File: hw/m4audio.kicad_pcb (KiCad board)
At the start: 2 copper layers, 49.7 x 49.7 mm, 95 parts, among them J1 JACK_TRS, J11 CONN_01X03, J2 JACK_TRS, J21 CONN_01X03, P1 CONN_01X02, P2 USB_OTG, P3 CONN_02X05, P4 CONN_01X08, P5 CONN_01X03, P6 CONN_01X04, U1 LD1117S33TR, U2 STM32F405RG, U3 AD8542, U4 WM8731, Y1 Crystal

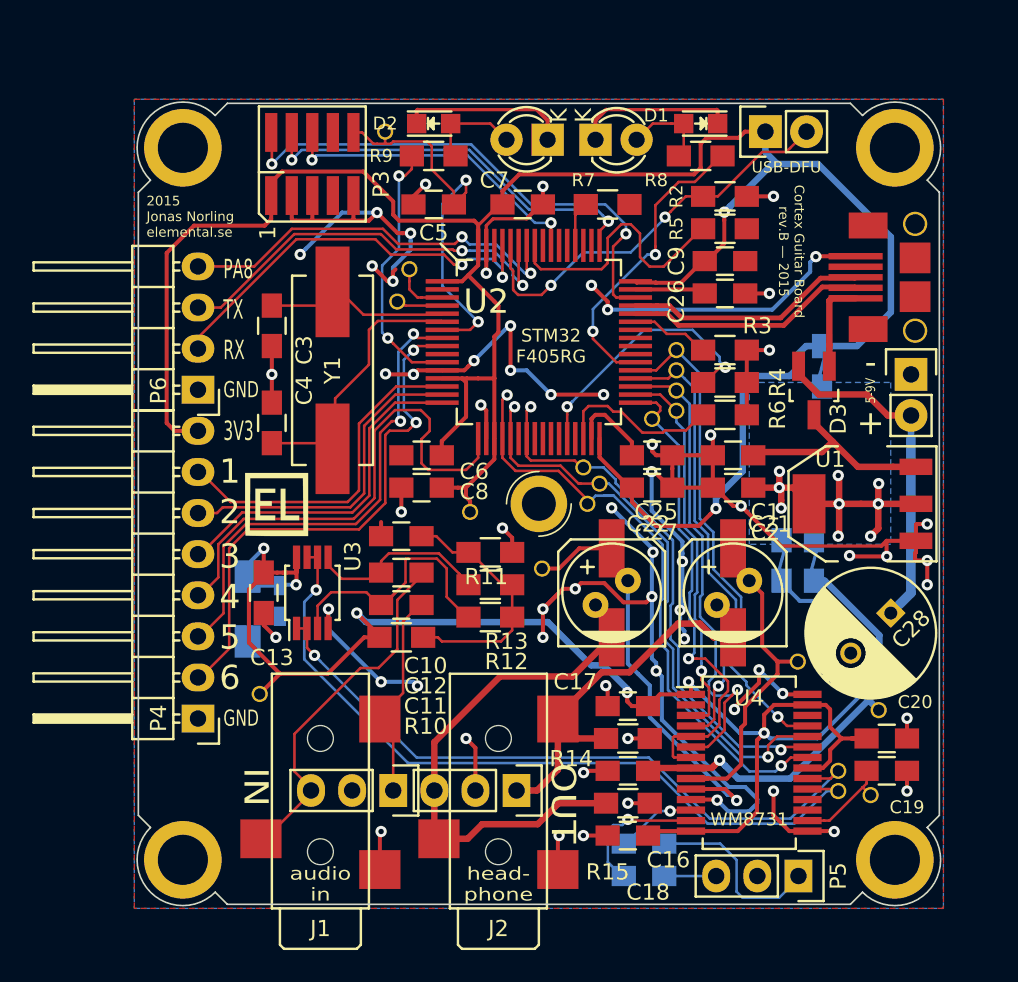
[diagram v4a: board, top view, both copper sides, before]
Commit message: Change LED footprints and resistors, RST header, hole in GND pad
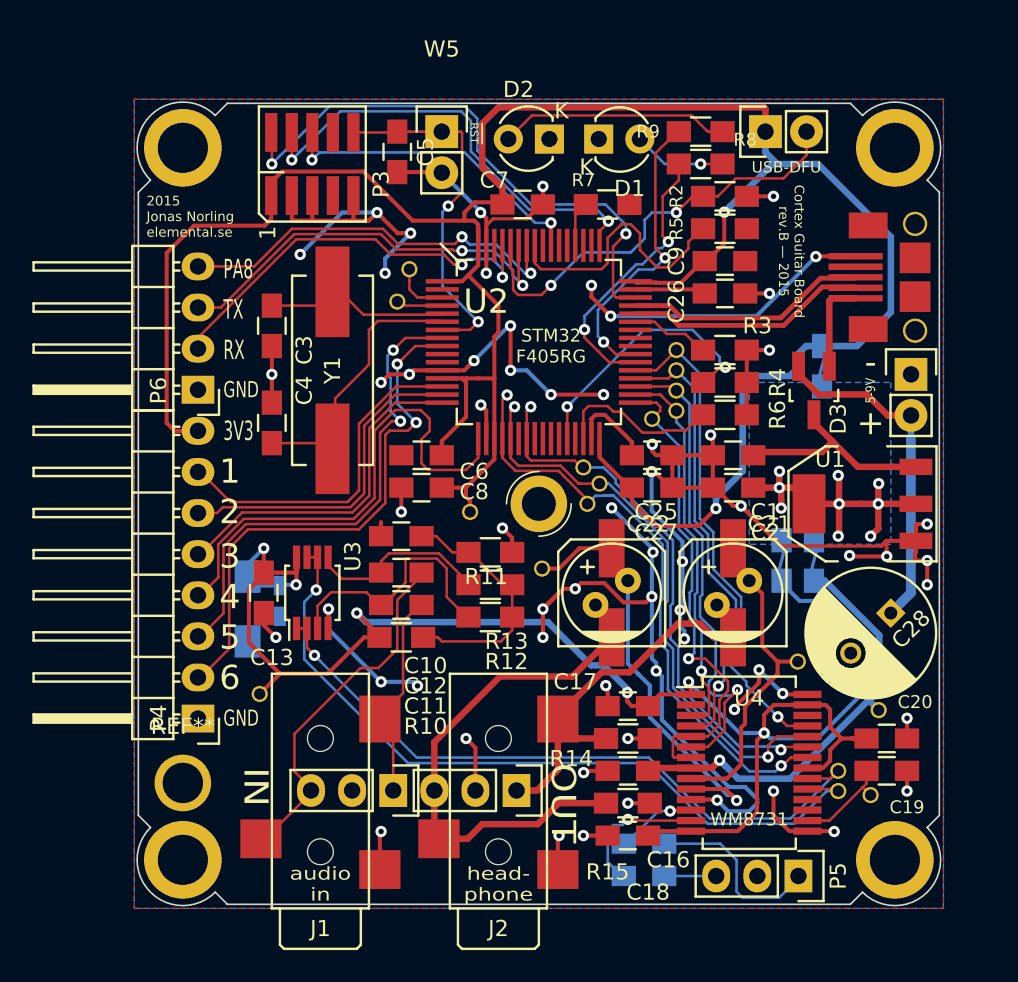
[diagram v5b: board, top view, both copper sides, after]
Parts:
- removed D11: green, LEDs:LED-3MM
- removed D21: orange, LEDs:LED-3MM
- removed G***: LOGO, elemental:elemental-25.4mm
- removed G***: LOGO, elemental:elemental-4mm
- removed G***: LOGO, Jonas_Gnomes:OSHW_4mm_mask
- removed G***: LOGO, elemental:elemental-4mm-mask
- removed the REF** at (130.0, 126.0)
- removed TP19: TST, Jonas_Connectors:TP_0.7mm
- added REF**: MountingHole_2-5mm, Mounting_Holes:MountingHole_2-5mm, F.Cu at (114.0, 132.2)
- added W5: TEST, Pin_Headers:Pin_Header_Straight_1x02, F.Cu at (130.0, 92.0)
- D1, D2: footprint LEDs:LED-0805 -> Footprints:LED-3MM
- moved R9 16.6 mm to (146.0, 92.0)
- moved D2 7.22 mm to (136.7, 92.5), turned to 180 degrees
- moved D1 6.37 mm to (139.7, 92.5), turned to 0 degrees
- moved C5 3.95 mm to (127.2, 93.2), turned to 270 degrees
- moved R8 0.50 mm to (146.0, 94.0), turned to 180 degrees
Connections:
- U2 pad 11: /LED2 -> Net-(U2-Pad11)
- U2 pad 39: Net-(U2-Pad39) -> /LED2
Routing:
- net GND: track 237.5 -> 221.9 mm, vias 64 -> 63
- net Net-(D2-Pad2): track 5.99 -> 14.3 mm
- net VDD: track 149.9 -> 157.6 mm
- net /SWCLK: track 25.1 -> 29.0 mm
- net /SWDIO: track 32.5 -> 35.6 mm
- net /NRST: track 24.7 -> 22.3 mm
- net /LED2: track 16.4 -> 18.6 mm
- net /BOOT0: track 25.3 -> 26.8 mm
- net /LED1: track 18.8 -> 17.6 mm
- net Net-(D1-Pad2): track 5.45 -> 6.20 mm, vias 0 -> 1
- net /SWO: track 19.7 -> 20.3 mm

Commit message: Redo power supply, split ground plane
Change to using two SOT-23-5 voltage regulators, one for analog and
one for digital. Split the ground plane so that digital and analog
meat at only one point, hoping to improve ground coupled noise
performance.

Update silkscreen texts to "rev.C".

Move silkscreen texts.
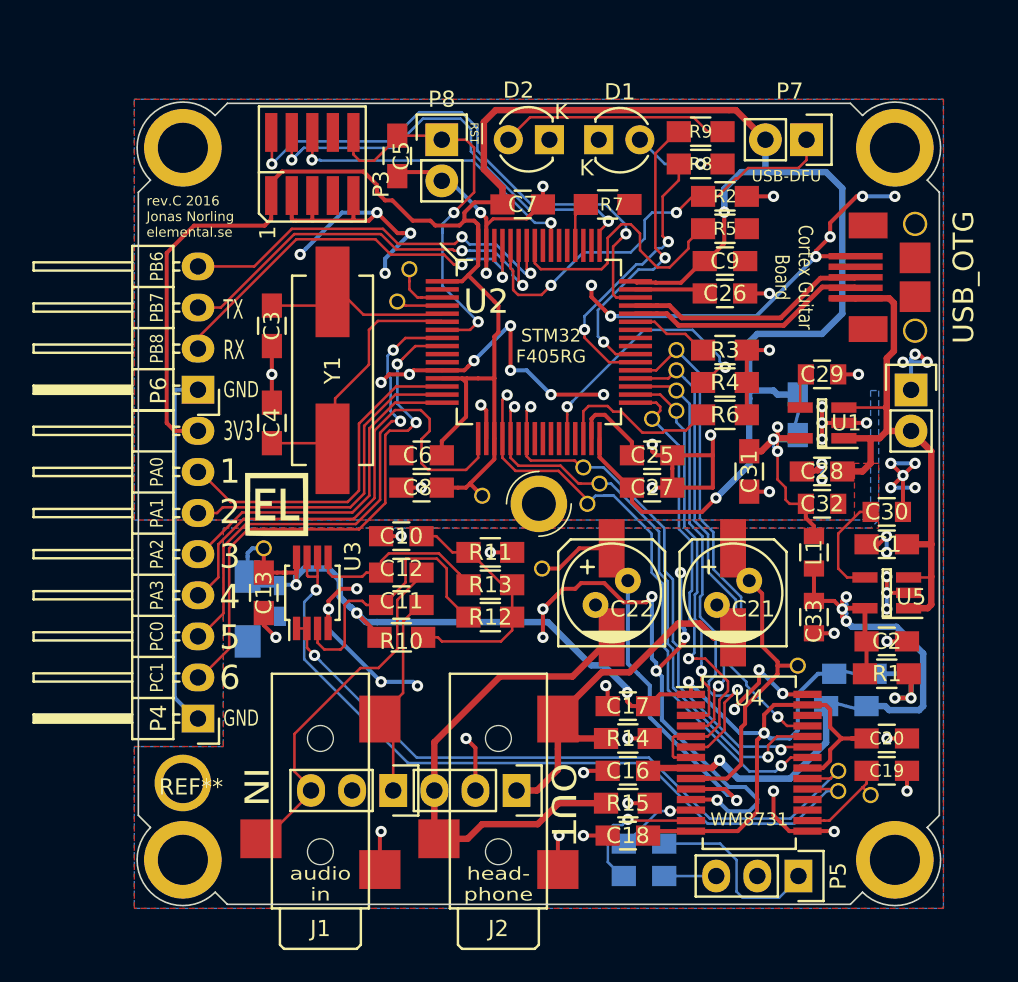
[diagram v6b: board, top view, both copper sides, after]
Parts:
- removed D3: SBAT54CLT1G, Housings_SOT-23_SOT-143_TSOT-6:SOT-23_Handsoldering
- removed TP9: TST, Jonas_Connectors:TP_0.7mm
- removed W1, W5: TEST, Pin_Headers:Pin_Header_Straight_1x02
- removed W2: V_A, Jonas_Connectors:net_tie_0805
- removed W3: V_D, Jonas_Connectors:net_tie_0805
- removed W4: V_HP, Jonas_Connectors:net_tie_0805
- added C29: 100p, Capacitors_SMD:C_0805, F.Cu at (153.5, 107.0)
- added C30: 100p, Capacitors_SMD:C_0805, F.Cu at (157.5, 115.5)
- added C31: 10u, Capacitors_SMD:C_0805_HandSoldering, F.Cu at (149.0, 113.0)
- added C32: DNP, Capacitors_SMD:C_0805, F.Cu at (153.5, 115.0)
- added C33: DNP, Capacitors_SMD:C_0805, F.Cu at (153.0, 122.0)
- added G***: LOGO, elemental:elemental-4mm, F.Cu at (119.8, 115.0)
- added G***: LOGO, elemental:elemental-25.4mm, B.Cu at (122.5, 107.2)
- added G***: LOGO, elemental:elemental-4mm-mask, B.Cu at (150.5, 99.8)
- added L1: DNP, Capacitors_SMD:C_0805, F.Cu at (153.0, 118.0)
- added P7: CONN_01X02, Pin_Headers:Pin_Header_Straight_1x02, F.Cu at (152.5, 92.5)
- added P8: CONN_01X02, Pin_Headers:Pin_Header_Straight_1x02, F.Cu at (130.0, 92.5)
- added R1: R, Resistors_SMD:R_0805_HandSoldering, F.Cu at (157.5, 125.5)
- added REF**: OSHW, Footprints:OSHW_4mm_mask, B.Cu at (146.5, 99.8)
- added REF**: gnome1, Jonas_Gnomes:gnome1, B.Cu at (136.0, 125.5)
- added TIE1: V_D, Jonas_Connectors:net_tie_0805, B.Cu at (152.0, 109.5)
- added TIE2: V_A, Jonas_Connectors:net_tie_0805, B.Cu at (155.5, 125.5)
- added TIE3: V_HP, Jonas_Connectors:net_tie_0805, B.Cu at (155.0, 127.5)
- added U5: AP2210K-3.3, Footprints:SOT-23-5_Handsoldering, F.Cu at (157.5, 120.5)
- C1: value 10u -> 10u16V
- C28: value DNP -> 10u16V; footprint Capacitors_ThroughHole:C_Radial_D8_L11.5_P3.5 -> Capacitors_SMD:C_0805_HandSoldering
- U1: value LD1117S33TR -> AP2210K-3.3; footprint SMD_Packages:SOT-223 -> Footprints:SOT-23-5_Handsoldering
- moved C2 13.4 mm to (157.5, 123.5), turned to 0 degrees
- moved C1 11.0 mm to (157.5, 117.5)
- moved C28 9.73 mm to (153.5, 113.0), turned to 180 degrees
- moved TP1 9.00 mm to (119.0, 117.8)
- moved U1 5.59 mm to (153.5, 110.0), turned to 180 degrees
- moved TP2 1.25 mm to (132.5, 114.5)
- moved P1 0.96 mm to (159.0, 108.0)
- moved C5 0.25 mm to (127.2, 93.5)
- moved TP15 0.25 mm to (152.0, 125.0)
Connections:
- C2 pad 1: /PWR_3V3 -> /APWR
- C28 pad 1: /VSUPPLY -> /PWR_5V
- P1 pad 2: /VSUPPLY -> /PWR_5V
- P2 pad 1: /USB_5V -> /PWR_5V
- U1 pad 1: GND -> /PWR_5V
- U1 pad 2: /PWR_3V3 -> GND
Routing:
- net GND: track 221.9 -> 253.0 mm, vias 63 -> 81
- net /PWR_5V: track 13.2 -> 39.7 mm
- net /APWR: track 0.00 -> 25.5 mm, vias 0 -> 3
- net /VSUPPLY: track 21.2 -> 0.00 mm
- net VAA: track 105.2 -> 85.0 mm, vias 6 -> 5
- net /PWR_3V3: track 20.0 -> 0.00 mm, vias 9 -> 0
- net /DPWR: track 0.00 -> 15.3 mm, vias 0 -> 3
- net HPVDD: track 27.0 -> 14.9 mm
- net Net-(R1-Pad2): track 0.00 -> 7.02 mm, vias 0 -> 2
- net /BYP2: track 0.00 -> 6.59 mm
- net /USB_5V: track 5.73 -> 0.00 mm
- net /NRST: track 22.3 -> 25.2 mm
- net /BYP1: track 0.00 -> 2.19 mm
- net VDD: track 157.6 -> 155.5 mm
- net /audio/OPINL: track 17.2 -> 19.0 mm
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- removed copper zone on B.Cu, net /PWR_3V3
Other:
- board text added: "Analog 3V3"
- board text added: "Cortex Guitar Board"
- board text added: "Cortex Guitar Board—rev.C-Jonas Norling 2016"
- board text added: "Digital 3V3"
- board text added: "PA0"
- board text added: "PA1"
- board text added: "PA2"
- board text added: "PA3"
- board text added: "PB6"
- board text added: "PB7"
- board text added: "PB8"
- board text added: "PC0"
- board text added: "PC1"
- board text added: "headphone 3V3"
- board text added: "rev.C 2016 Jonas Norling elemental.se"
- board text removed: "+"
- board text removed: "-"
- board text removed: "2015 Jonas Norling elemental.se"
- board text removed: "5-9V"
- board text removed: "Cortex Guitar Board rev.B — 2015"
- board text removed: "Cortex Guitar Board—rev.B-Jonas Norling 2015"
- board text removed: "HPVDD"
- board text removed: "PA8"
- board text removed: "analog"
- board text removed: "digital"
- board text removed: "headphone"

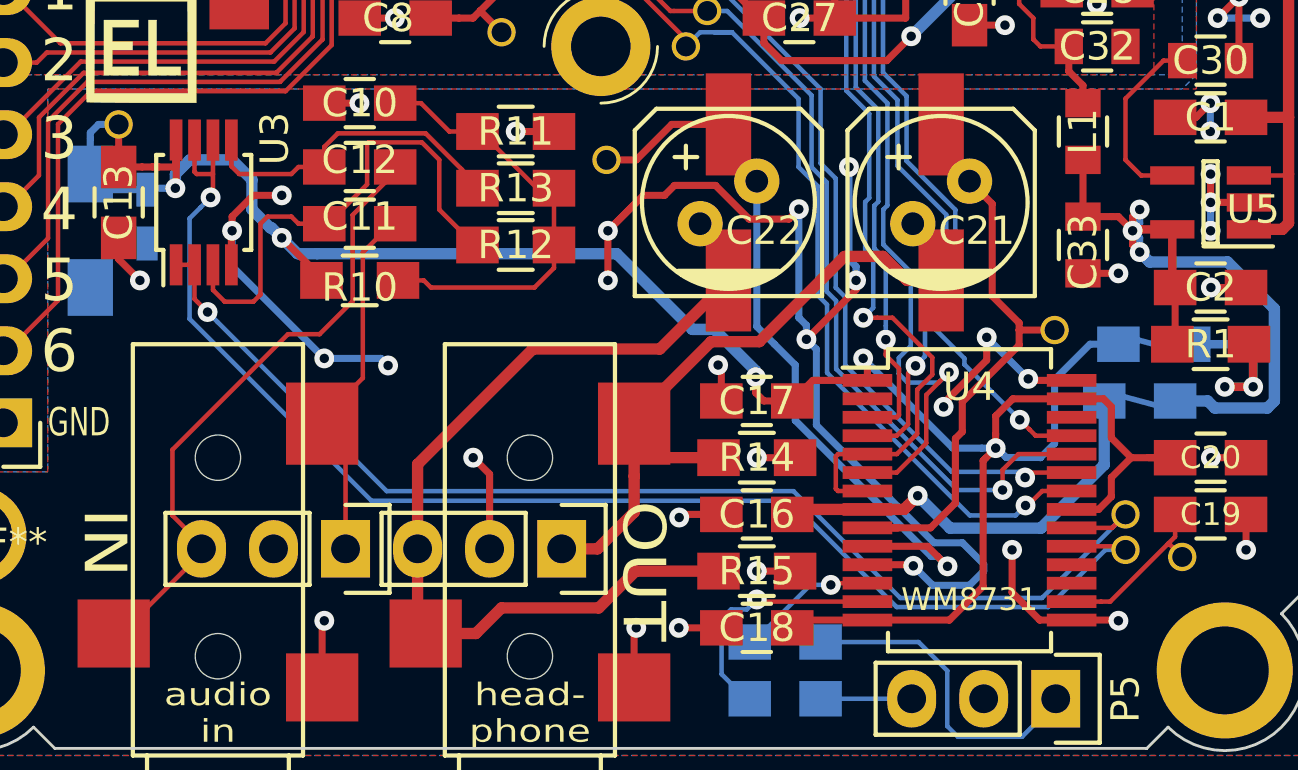
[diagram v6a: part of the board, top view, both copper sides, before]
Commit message: Net tie to bypass the pre-amp
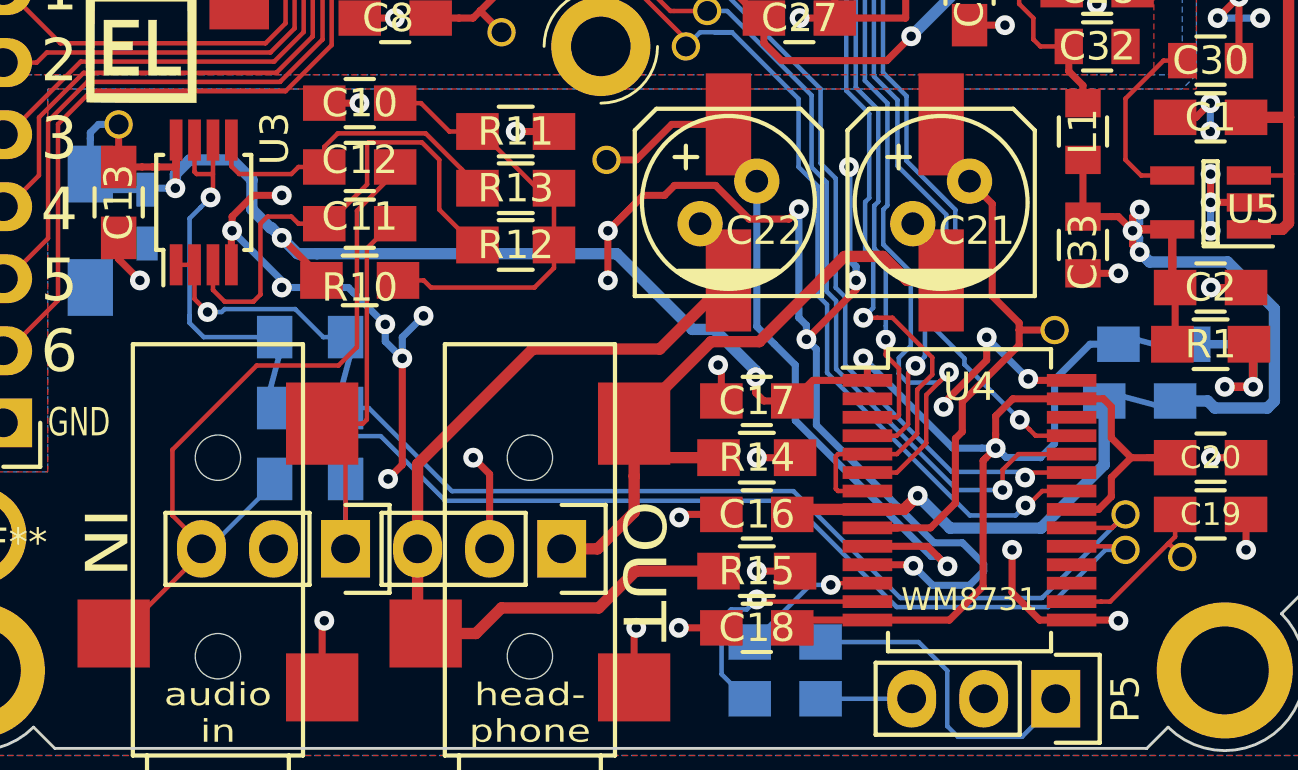
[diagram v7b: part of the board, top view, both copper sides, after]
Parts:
- added TIE4: CONN_01X03, Jonas_Connectors:net_tie_3_0805, B.Cu at (127.0, 125.2)
- added TIE5: CONN_01X03, Jonas_Connectors:net_tie_3_0805, B.Cu at (124.5, 125.2)
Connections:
- U3 pad 1: /audio/ADCL -> /audio/OPOUTL
- U3 pad 2: /audio/ADCL -> /audio/OPOUTL
- U3 pad 6: /audio/ADCR -> /audio/OPOUTR
- U3 pad 7: /audio/ADCR -> /audio/OPOUTR
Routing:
- net /audio/ADCR: track 48.5 -> 36.0 mm, vias 1 -> 0
- net /audio/OPOUTR: track 0.00 -> 11.9 mm, vias 0 -> 1
- net /audio/ADCL: track 42.4 -> 33.6 mm, vias 1 -> 0
- net /audio/OPOUTL: track 0.00 -> 7.82 mm, vias 0 -> 1
- net GND: track 253.0 -> 259.4 mm, vias 81 -> 84
- net /audio/AIN_R: track 22.2 -> 26.9 mm
- net /audio/AIN_L: track 12.9 -> 16.3 mm
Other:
- board text added: "jack"
- board text added: "preamp"
